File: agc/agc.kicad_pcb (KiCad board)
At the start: 2 copper layers, 72.4 x 59.1 mm, 63 parts, among them J5 SIL10, K1 TR, K10 HVMON, K11 HVMON, K2 TR, K3 VIN, K4 VOUT_TR, K5 TR, K6 TR, K7 HVMON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

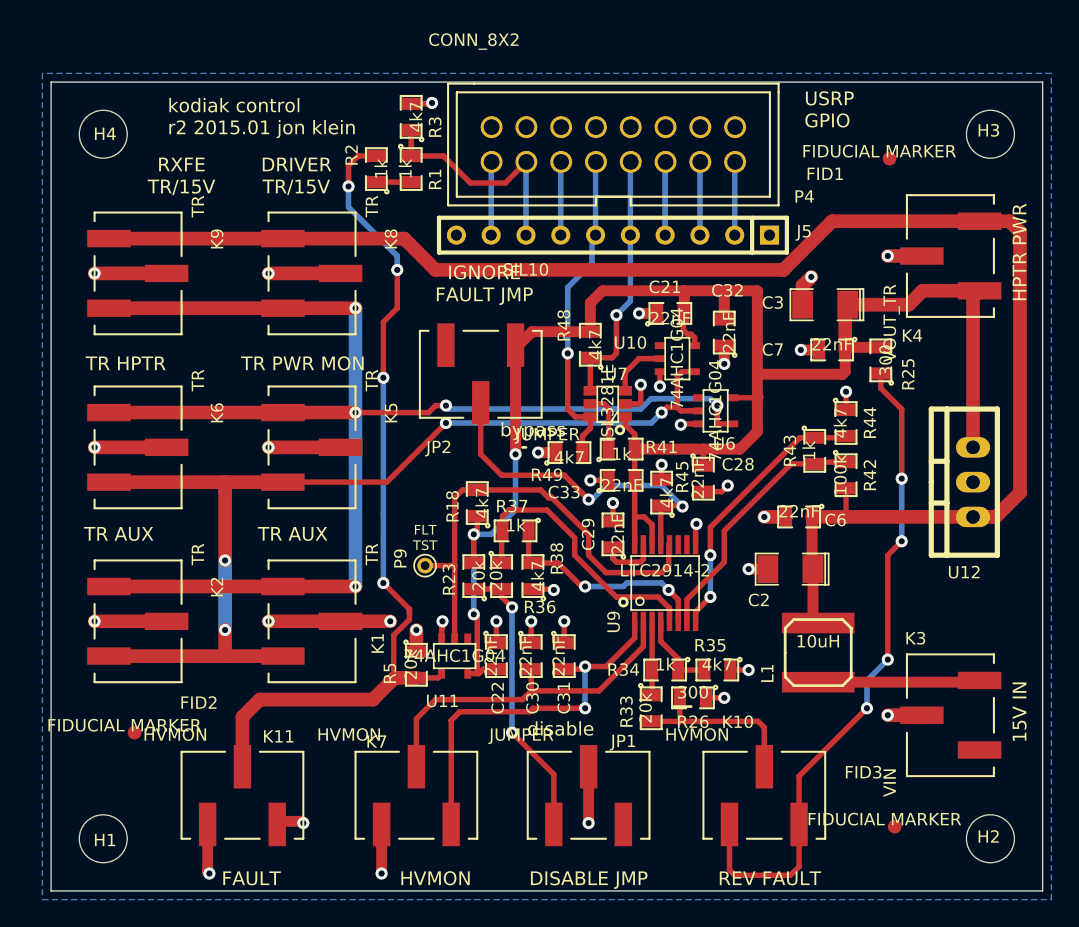
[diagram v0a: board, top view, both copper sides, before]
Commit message: updated schematic with distributor part numbers
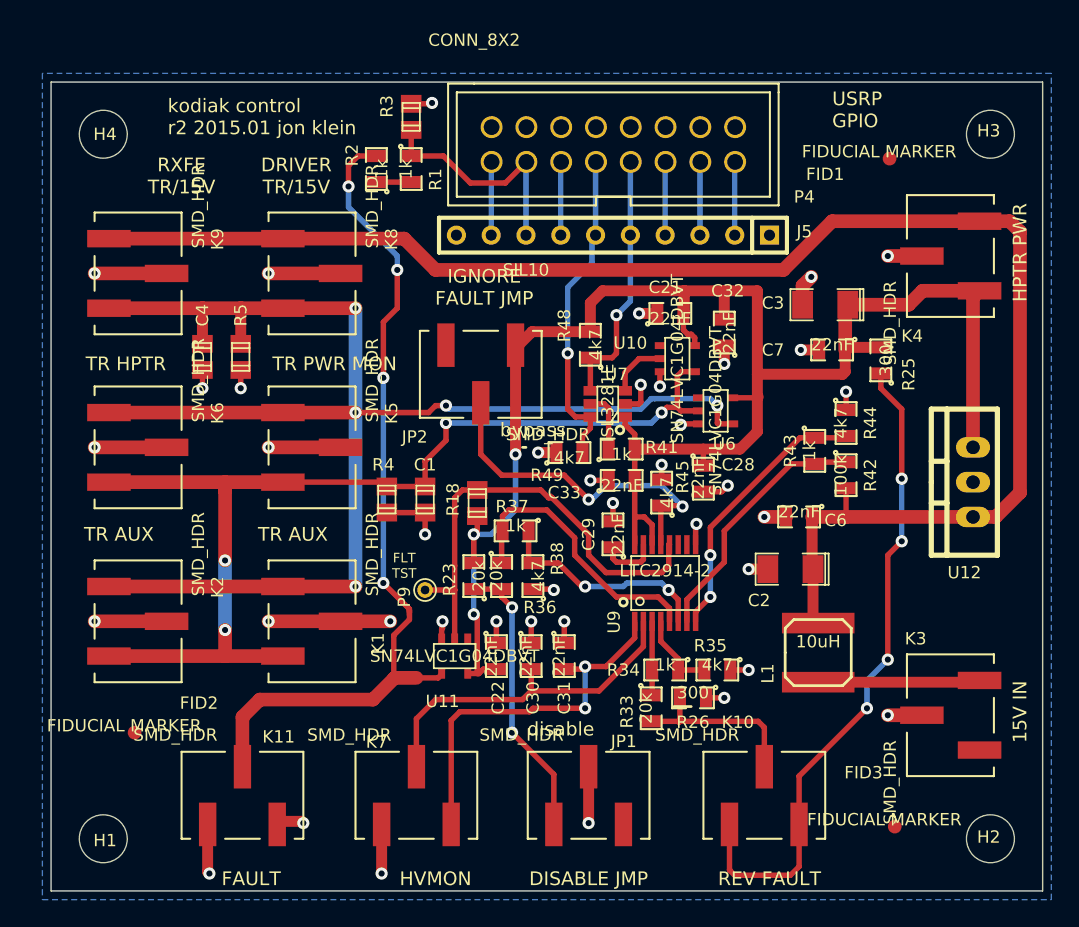
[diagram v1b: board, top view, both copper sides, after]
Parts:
- added C1: 22pF, smd_capacitors:c_0805, F.Cu at (60.2, 83.8)
- added C4: 22pF, smd_capacitors:c_0805, F.Cu at (43.9, 73.4)
- added R4: 4k7, smd_capacitors:c_0805, F.Cu at (57.4, 83.8)
- C2, C3: value 20 uF -> 22 uF
- JP1, JP2: value JUMPER -> SMD_HDR
- K1, K2, K5, K6, K8, K9: value TR -> SMD_HDR
- K10, K11, K7: value HVMON -> SMD_HDR
- K3: value VIN -> SMD_HDR
- K4: value VOUT_TR -> SMD_HDR
- P9: value COUPLED_TEST -> TESTPOINT
- R18, R3: footprint SMD_Packages:SMD-0805 -> smd_capacitors:c_0805
- R5: value 20k -> 4k7; footprint SMD_Packages:SMD-0805 -> smd_capacitors:c_0805
- U10, U11, U6: value 74AHC1G04 -> SN74LVC1G04DBVT
- moved R5 25.9 mm to (46.7, 73.4)
- moved P9 1.78 mm to (60.2, 90.4)
- turned R18 to 270 degrees
- turned R3 to 270 degrees
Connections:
- R5 pad 2: /~FAULT -> /TX
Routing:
- net /TX: track 103.6 -> 109.3 mm
- net GND: track 90.4 -> 95.9 mm, vias 38 -> 40
- net /~TX: track 88.9 -> 90.9 mm

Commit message: updated agc to recent version of kicad - removed vestigial inner layers and fixed schematic for smaller passives
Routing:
- net (no net): track 34.9 -> 0.00 mm

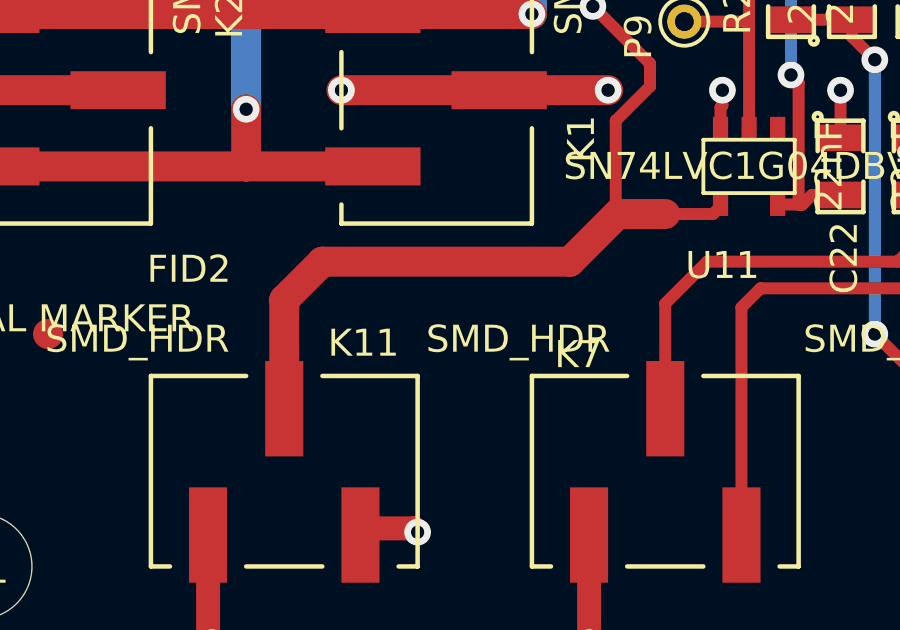
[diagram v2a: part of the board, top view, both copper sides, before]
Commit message: added breakout board for usrp dio - allow cases to be closed during operation by routing all io through dio header
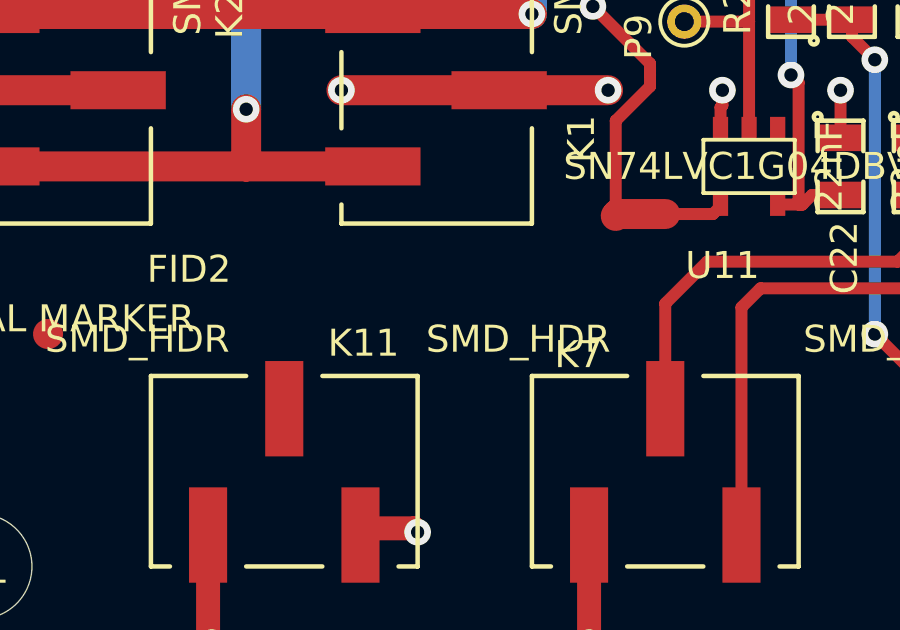
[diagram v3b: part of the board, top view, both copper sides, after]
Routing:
- net /~FAULT: track 62.8 -> 46.8 mm

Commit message: committing modified files, I forget.., probably dfm
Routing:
- net /~FAULT: track 46.8 -> 62.5 mm

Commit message: finalized driveramp, rxfe, and control for macrofab
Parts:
- R42: value 100k -> 133k
- U9: value LTC2914-2 -> ADM2914-2
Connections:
- net Net-(J5-Pad3) renamed /DISABLE
- K11 pad 2: /~FAULT -> /FAULT
- K3 pad 1: (no net) -> Net-(K3-Pad1)
- U9 pad 10: (no net) -> Net-(U9-Pad10)
- U9 pad 11: (no net) -> Net-(U9-Pad11)
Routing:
- net /FAULT: track 33.9 -> 57.6 mm
- net /~FAULT: track 62.5 -> 44.9 mm
- net GND: track 95.9 -> 92.1 mm, vias 40 -> 39

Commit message: added dfm changes from fab, I think
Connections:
- K9 pad 3: /TX -> /~TX
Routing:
- net /~TX: track 90.9 -> 108.6 mm
- net /TX: track 109.3 -> 102.7 mm

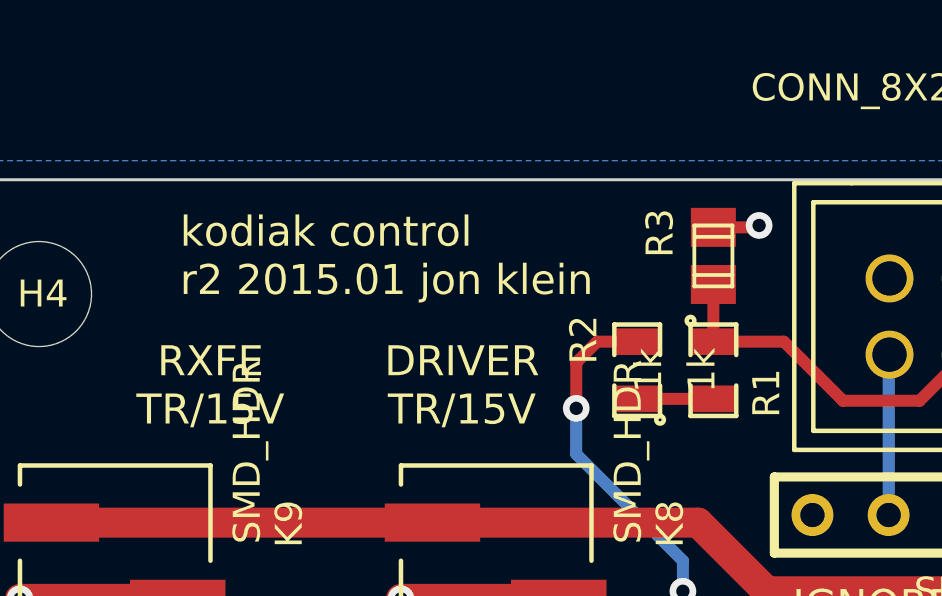
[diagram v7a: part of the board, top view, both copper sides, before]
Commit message: added tvs diodes to external connections on mcm_rxfe
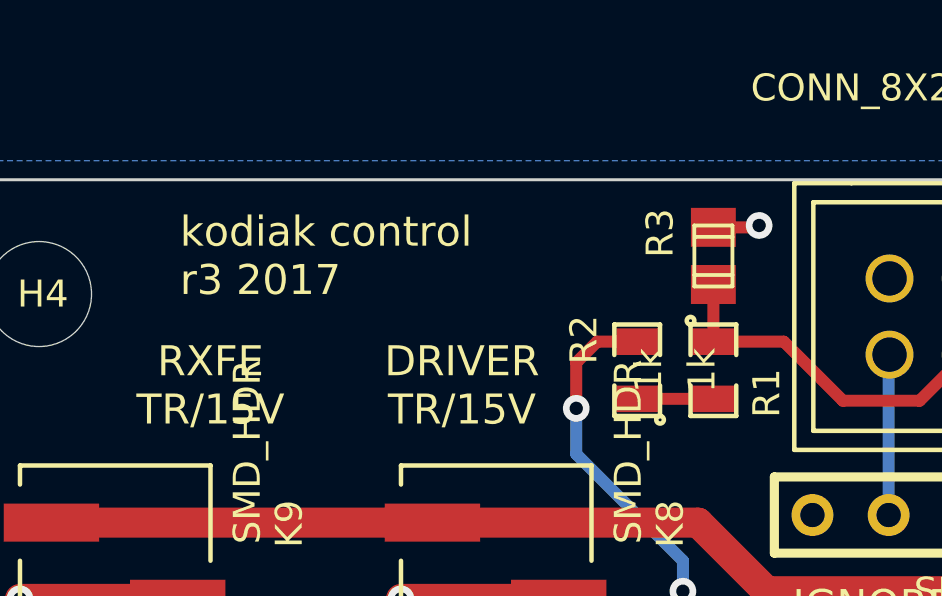
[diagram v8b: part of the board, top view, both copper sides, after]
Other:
- board text added: "kodiak control r3 2017"
- board text removed: "kodiak control r2 2015.01 jon klein"
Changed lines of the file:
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@@
-(kicad_pcb (version 4) (host pcbnew 4.0.2-2.fc24-product)
+(kicad_pcb (version 4) (host pcbnew 4.0.4-1.fc24-product)
   (general
     (links 140)
     (no_connects 0)
-    (area 30.971216 49.2075 107.204785 114.48376)
+    (area 31.058716 49.3825 107.117285 114.57376)
     (thickness 1.6)
     (drawings 27)
@@
     (effects (font (size 1 1) (thickness 0.2)))
   )
-  (gr_text "kodiak control \nr2 2015.01 jon klein" (at 41.402 55.88) (layer F.SilkS)
+  (gr_text "kodiak control \nr3 2017" (at 41.402 55.88) (layer F.SilkS)
     (effects (font (size 1 1) (thickness 0.25)) (justify left))
   )
